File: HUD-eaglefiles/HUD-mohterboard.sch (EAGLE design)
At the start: 74 parts, among them U1 LM317, U2 ATMEGA328P_TQFP

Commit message: finalised all circuits and added comments on the motherboard circuit
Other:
- note added: "# All connectors that are going to be connected to the display board must be soldered"
- note added: "# Excese analog and digital pins each has two connectors, one is only holes for final"
- note added: "# Parts that have the value "holes" in the BOM file should only be holes."
- note added: "This is the motherboard circuit that contains the controlling circuits and connections."
- note added: "connection, the other is female header for debugging. These are soldered close to"
- note added: "eatch other."
- note added: "next to each others"

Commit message: modified the shift registers packaging
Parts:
- SR_D0, SR_D1, SR_D2: value 74595 -> 74LS595N; device SparkFun-DigitalIC:74595 -> SparkFun-DigitalIC:74LS595N
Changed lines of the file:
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@@
 <part name="DOUT" library="SparkFun-Connectors" deviceset="M05" device="PTH" value="female_header"/>
 <part name="AOUT_H" library="SparkFun-Connectors" deviceset="M06" device="SILK_FEMALE_PTH" value="holes"/>
-<part name="SR_D0" library="SparkFun-DigitalIC" deviceset="74*595" device=""/>
+<part name="SR_D0" library="SparkFun-DigitalIC" deviceset="74*595" device="N" technology="LS" value="74LS595N"/>
 <part name="GND10" library="SparkFun-Aesthetics" deviceset="GND" device=""/>
 <part name="COM_SERIAL" library="SparkFun-Connectors" deviceset="M02" device="PTH" value="male_header"/>
-<part name="SR_D1" library="SparkFun-DigitalIC" deviceset="74*595" device=""/>
+<part name="SR_D1" library="SparkFun-DigitalIC" deviceset="74*595" device="N" technology="LS" value="74LS595N"/>
 <part name="GND11" library="SparkFun-Aesthetics" deviceset="GND" device=""/>
-<part name="SR_D2" library="SparkFun-DigitalIC" deviceset="74*595" device=""/>
+<part name="SR_D2" library="SparkFun-DigitalIC" deviceset="74*595" device="N" technology="LS" value="74LS595N"/>
 <part name="GND12" library="SparkFun-Aesthetics" deviceset="GND" device=""/>
 <part name="QA0" library="SparkFun-DiscreteSemi" deviceset="TRANSISTOR_NPN" device="P2N2222A"/>

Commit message: modified the reset button into through hole packaging
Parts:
- RESET: device SmartPrj:TS42 -> SparkFun-Retired:TAC_SWITCHPTH
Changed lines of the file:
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@@
 <part name="JP1" library="SparkFun-Connectors" deviceset="M02" device="PTH" value="Pwr_in"/>
 <part name="U2" library="SparkFun-DigitalIC" deviceset="ATMEGA328P_TQFP" device="" value="ATMEGA328P_TQFP"/>
-<part name="RESET" library="SmartPrj" deviceset="TS42" device="" value="TS42031-160R-TR-7260"/>
+<part name="RESET" library="SparkFun-Retired" deviceset="TAC_SWITCH" device="PTH" value="TS42031-160R-TR-7260"/>
 <part name="GND9" library="SparkFun-Aesthetics" deviceset="GND" device=""/>
 <part name="R5" library="SparkFun-Resistors" deviceset="RESISTOR" device="PTH-1/4W" value="10K"/>
@@
 <attribute name="VALUE" x="193.04" y="187.96" size="1.778" layer="96" font="vector"/>
 </instance>
-<instance part="RESET" gate="G$1" x="167.64" y="223.52" smashed="yes">
+<instance part="RESET" gate="S" x="167.64" y="223.52" smashed="yes" rot="R90">
 <attribute name="NAME" x="161.29" y="220.98" size="1.778" layer="95" font="vector" rot="R90"/>
-<attribute name="VALUE" x="173.99" y="226.695" size="1.778" layer="96" font="vector" rot="R270"/>
+<attribute name="VALUE" x="173.99" y="212.725" size="1.778" layer="96" font="vector" rot="R90"/>
 </instance>
 <instance part="GND9" gate="1" x="170.18" y="210.82" smashed="yes">
@@
 <pinref part="GND9" gate="1" pin="GND"/>
 <wire x1="170.18" y1="213.36" x2="170.18" y2="215.9" width="0.1524" layer="91"/>
-<pinref part="RESET" gate="G$1" pin="2"/>
+<pinref part="RESET" gate="S" pin="2"/>
 <wire x1="170.18" y1="215.9" x2="170.18" y2="218.44" width="0.1524" layer="91"/>
-<pinref part="RESET" gate="G$1" pin="1"/>
+<pinref part="RESET" gate="S" pin="1"/>
 <wire x1="167.64" y1="218.44" x2="167.64" y2="215.9" width="0.1524" layer="91"/>
 <wire x1="167.64" y1="215.9" x2="170.18" y2="215.9" width="0.1524" layer="91"/>
@@
 <net name="RESET_WIRE" class="0">
 <segment>
-<pinref part="RESET" gate="G$1" pin="3"/>
+<pinref part="RESET" gate="S" pin="3"/>
 <wire x1="167.64" y1="228.6" x2="167.64" y2="231.14" width="0.1524" layer="91"/>
 <wire x1="167.64" y1="231.14" x2="170.18" y2="231.14" width="0.1524" layer="91"/>
-<pinref part="RESET" gate="G$1" pin="4"/>
+<pinref part="RESET" gate="S" pin="4"/>
 <wire x1="170.18" y1="228.6" x2="170.18" y2="231.14" width="0.1524" layer="91"/>
 <pinref part="U2" gate="U$1" pin="PC6(/RESET)"/>

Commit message: changed the transistors to uln2003 (a transistor array) and rewired the schematic
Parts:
- removed C1: 100uF, SparkFun:CAP_POLPTH1
- removed D1: 1N4001, SparkFun:DIODEPTH
- removed DIS_PWR_SELECT: JUMPER-3PTH, SparkFun-Retired:JUMPER-3PTH
- removed F1: 500mA, SparkFun:PTCPTH
- removed LED2: Power, SparkFun-Nate:LED5MM
- removed QA0, QA1, QA2, QB0, QB1, QB2, QC0, QC1, QC2, QD0, QD1, QD2, QE0, QE1, QE2, QF0, QF1, QF2, QG0, QG1, QG2: (no value), SparkFun-DiscreteSemi:TRANSISTOR_NPNP2N2222A
- removed R1: 240, SparkFun:RESISTORPTH1
- removed R10, R11, R12, R13, R14, R15, R16, R17, R18, R19, R20, R21, R22, R23, R24, R25, R26, R27, R6, R7, R8, R9: 1K, SparkFun-Resistors:RESISTORPTH-1/4W
- removed R2: 390, SparkFun:RESISTORPTH1
- removed R3, R4: 330, SparkFun:RESISTORPTH1
- removed S1: On/Off, SparkFun:SWITCH-SPSTPTH
- removed S2: Voltage, SparkFun:SWITCH-SPSTPTH
- removed U1: LM317, SparkFun:V_REG_317SINK
- added IC1: 7805TV, linear:7805TV
- added TA_D0, TA_D1, TA_D2: ULN2003AN, uln-udn:ULN2003AN
- added Y1: 4MHz, SparkFun-FreqCtrl:RESONATOR4MHZ
- C2: value 10uF -> 0.47u; device SparkFun:CAP_POLPTH2 -> SparkFun-Passives:CAP0805
- C3: value 0.1uF -> 33u; device SparkFun:CAPPTH2 -> SparkFun-Passives:CAP0805
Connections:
- removed net 12VOUT: DIS_PWR_SELECT.3, R27.2
- removed net DISPLAY_PWR-OUT: DIS_PWR_SELECT.2, PWR_PINS_OUT.1
- removed net N$20: QA1.B, R13.2
- removed net N$21: QC1.B, R15.2
- removed net N$22: QD1.B, R16.2
- removed net N$23: QE1.B, R17.2
- removed net N$24: QF1.B, R18.2
- removed net N$25: QB1.B, R14.2
- removed net N$26: QG1.B, R19.2
- removed net N$27: D1_IN.4, QD1.C
- removed net N$28: D1_IN.3, QC1.C
- removed net N$31: D1_IN.5, QE1.C
- removed net N$34: QC0.B, R8.2
- removed net N$35: QD0.B, R9.2
- removed net N$36: QE0.B, R10.2
- removed net N$37: QF0.B, R11.2
- removed net N$38: QB0.B, R7.2
- removed net N$39: QG0.B, R12.2
- removed net N$40: D0_IN.4, QD0.C
- removed net N$41: D0_IN.3, QC0.C
- removed net N$42: D0_IN.2, QB0.C
- removed net N$44: D0_IN.5, QE0.C
- removed net N$45: D0_IN.6, QF0.C
- removed net N$47: QA2.B, R20.2
- removed net N$48: QC2.B, R22.2
- removed net N$49: QD2.B, R23.2
- removed net N$50: QE2.B, R24.2
- removed net N$51: QF2.B, R25.2
- removed net N$52: QB2.B, R21.2
- removed net N$53: QG2.B, R26.2
- removed net N$54: D2_IN.4, QD2.C
- removed net PWRIN: JP1.2, S1.P
- removed net RAW: C1.+, F1.2, R27.1, U1.IN
- new net N$10: D1_IN.5, TA_D1.O5
- new net N$11: D2_IN.4, TA_D2.O4
- new net N$3: D0_IN.2, TA_D0.O2
- new net N$7: D0_IN.6, TA_D0.O6
- new net N$9: D1_IN.4, TA_D1.O4
- new net VS: C2.1, IC1.VI, JP1.2, PWR_PINS_OUT.1
- net A0: now also TA_D0.I1; no longer R6.1
- net A1: now also TA_D1.I1; no longer R13.1
- net A2: now also TA_D2.I1; no longer R20.1
- net B0: now also TA_D0.I2; no longer R7.1
- net B1: now also TA_D1.I2; no longer R14.1
- net B2: now also TA_D2.I2; no longer R21.1
- net C0: now also TA_D0.I3; no longer R8.1
- net C1: now also TA_D1.I3; no longer R15.1
- net C2: now also TA_D2.I3; no longer R22.1
- net D0: now also TA_D0.I4; no longer R9.1
- net D1: now also TA_D1.I4; no longer R16.1
- net D2: now also TA_D2.I4; no longer R23.1
- net E0: now also TA_D0.I5; no longer R10.1
- net E1: now also TA_D1.I5; no longer R17.1
- net E2: now also TA_D2.I5; no longer R24.1
- net F0: now also TA_D0.I6; no longer R11.1
- net F1: now also TA_D1.I6; no longer R18.1
- net F2: now also TA_D2.I6; no longer R25.1
- net G0: now also TA_D0.I7; no longer R12.1
- net G1: now also TA_D1.I7; no longer R19.1
- net G2: now also TA_D2.I7; no longer R26.1
- net GND: now also C2.2, IC1.GND, TA_D0.GND, TA_D1.GND, TA_D2.GND, Y1.2; no longer C1.-, C2.-, LED2.C, QA0.E, QA1.E, QA2.E, QB0.E, QB1.E, QB2.E, QC0.E, QC1.E, QC2.E, QD0.E, QD1.E, QD2.E, QE0.E, QE1.E, QE2.E, QF0.E, QF1.E, QF2.E, QG0.E, QG1.E, QG2.E, R3.1, S2.S
- net N$1: now also U2.PB6(XTAL1/TOSC1), Y1.1; no longer D1.C, F1.1
- net N$2: now also U2.PB7(XTAL2/TOSC2), Y1.3; no longer D1.A, S1.S
- net N$29: now also TA_D1.O2; no longer QB1.C
- net N$30: now also TA_D1.O1; no longer QA1.C
- net N$32: now also TA_D1.O6; no longer QF1.C
- net N$33: now also TA_D1.O7; no longer QG1.C
- net N$4: now also D0_IN.3, TA_D0.O3; no longer R2.1, R3.2, S2.P
- net N$43: now also TA_D0.O1; no longer QA0.C
- net N$46: now also TA_D0.O7; no longer QG0.C
- net N$5: now also D0_IN.4, TA_D0.O4; no longer R1.1, R2.2, U1.ADJ
- net N$55: now also TA_D2.O3; no longer QC2.C
- net N$56: now also TA_D2.O2; no longer QB2.C
- net N$57: now also TA_D2.O1; no longer QA2.C
- net N$58: now also TA_D2.O5; no longer QE2.C
- net N$59: now also TA_D2.O6; no longer QF2.C
- net N$6: now also D0_IN.5, TA_D0.O5; no longer QA0.B, R6.2
- net N$60: now also TA_D2.O7; no longer QG2.C
- net N$8: now also D1_IN.3, TA_D1.O3; no longer LED2.A, R4.1
- net VCC: now also IC1.VO; no longer C2.+, DIS_PWR_SELECT.1, R1.2, R4.2, U1.OUT
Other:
- note added: "3"
- note removed: "2"
- note removed: "Display Power Out"
- moved on the sheet: C3, D0_IN, D1_IN, D2_IN, JP1, PWR_PINS_OUT, RESET

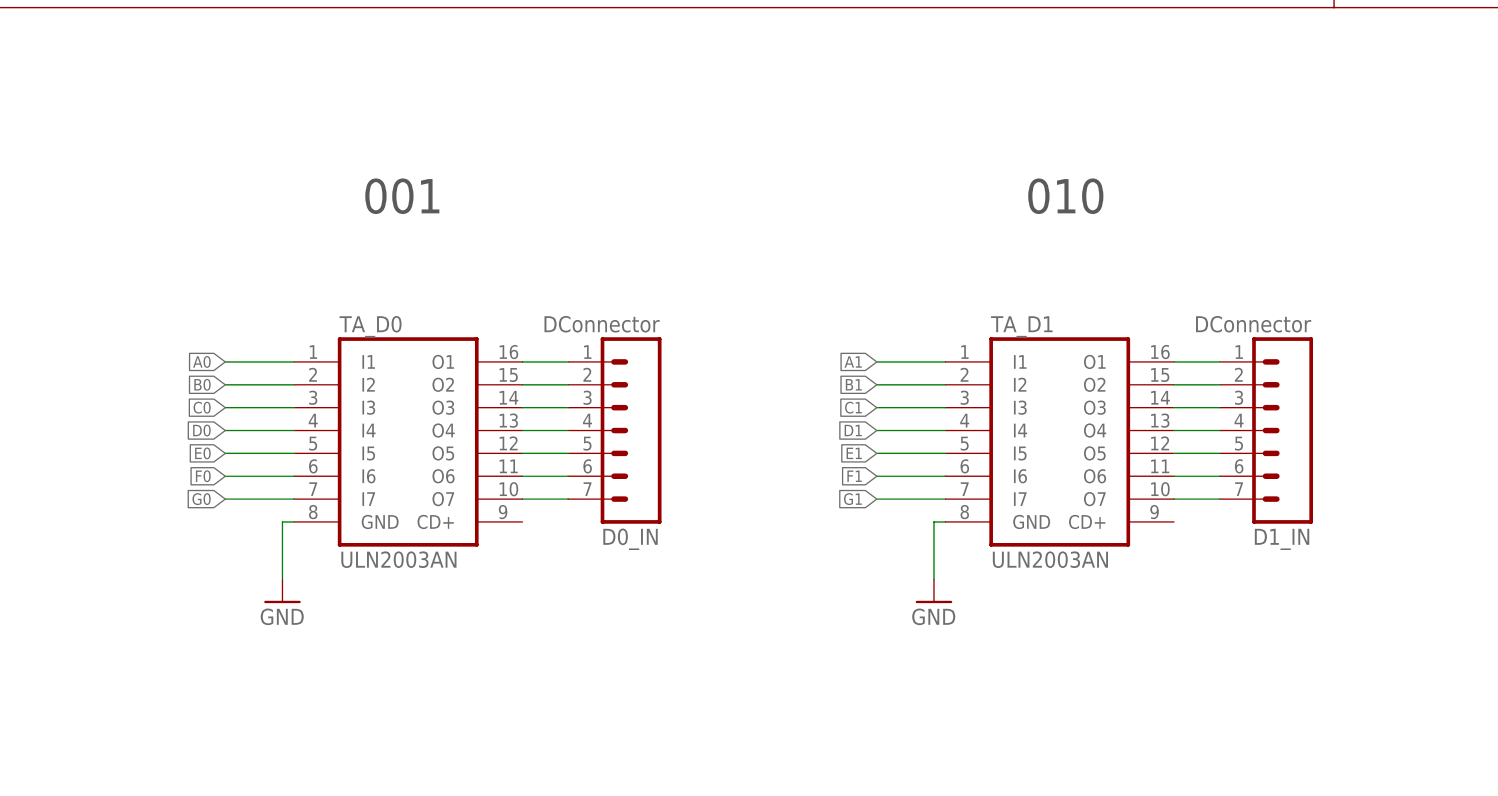
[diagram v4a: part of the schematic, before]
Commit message: added the pins mapping
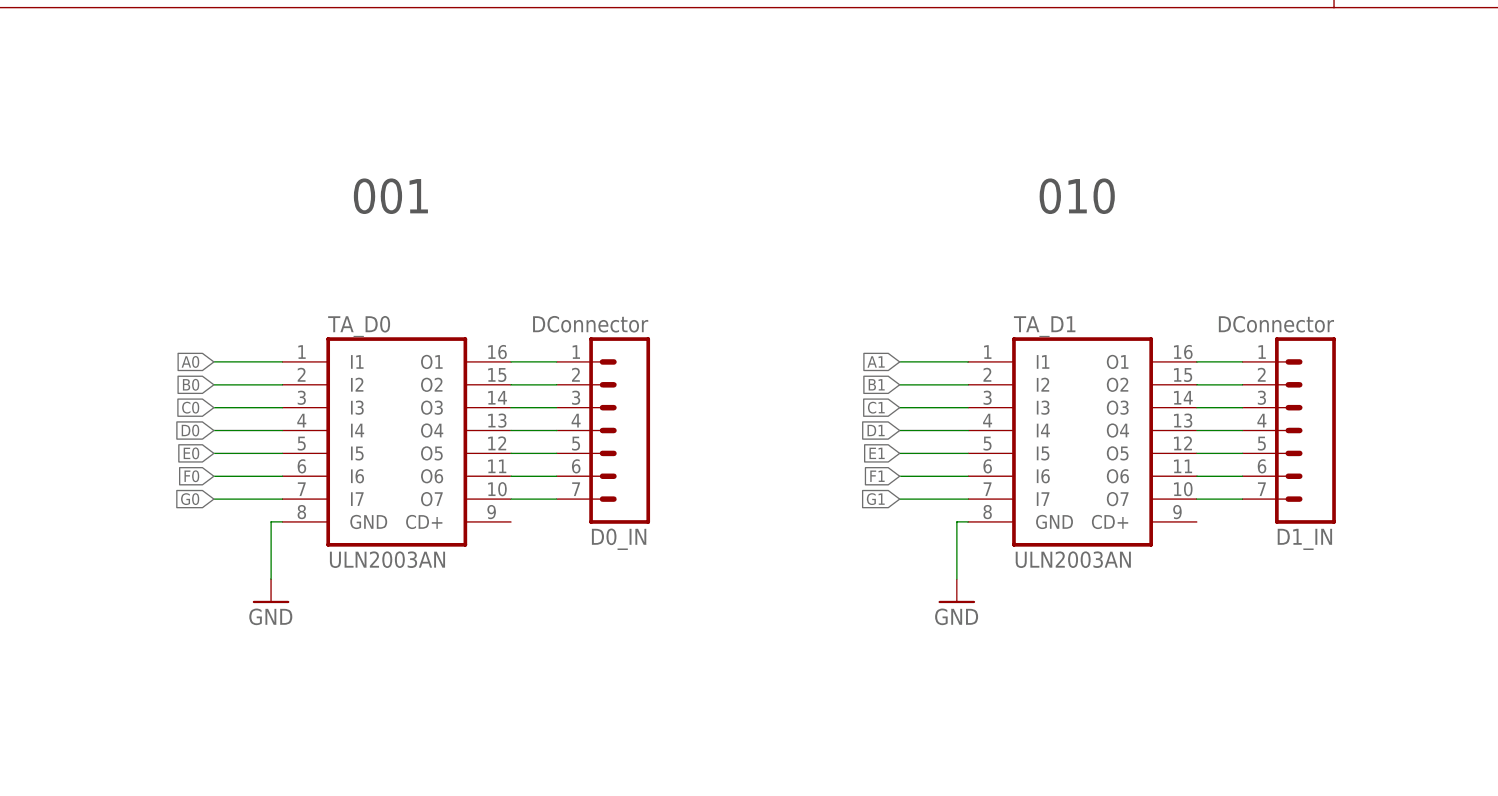
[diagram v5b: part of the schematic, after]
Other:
- note added: "OBD_RX -> D2 OBD_TX -> D3 SR_CLK -> D4 SR_SDATA -> D5 CE_D0 -> D6 CE_D1 -> D7 CE_D2 -> D8"
- moved on the sheet: D0_IN, D1_IN, TA_D0, TA_D1

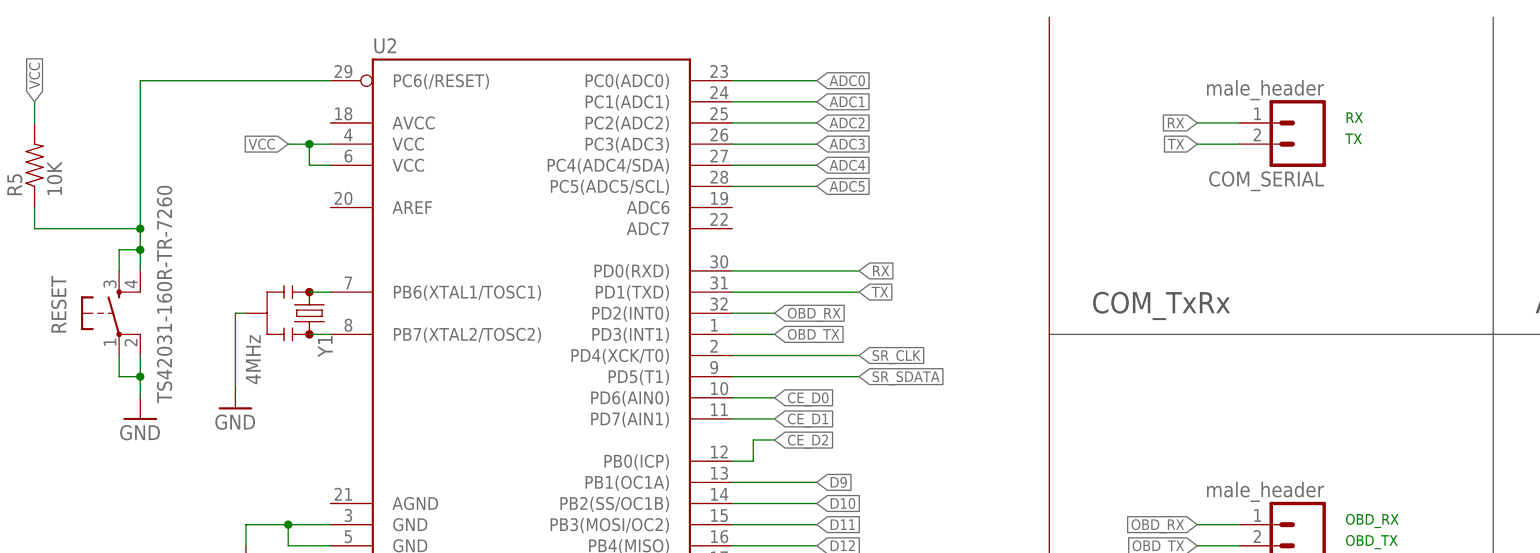
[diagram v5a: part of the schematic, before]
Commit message: fixed the serial port
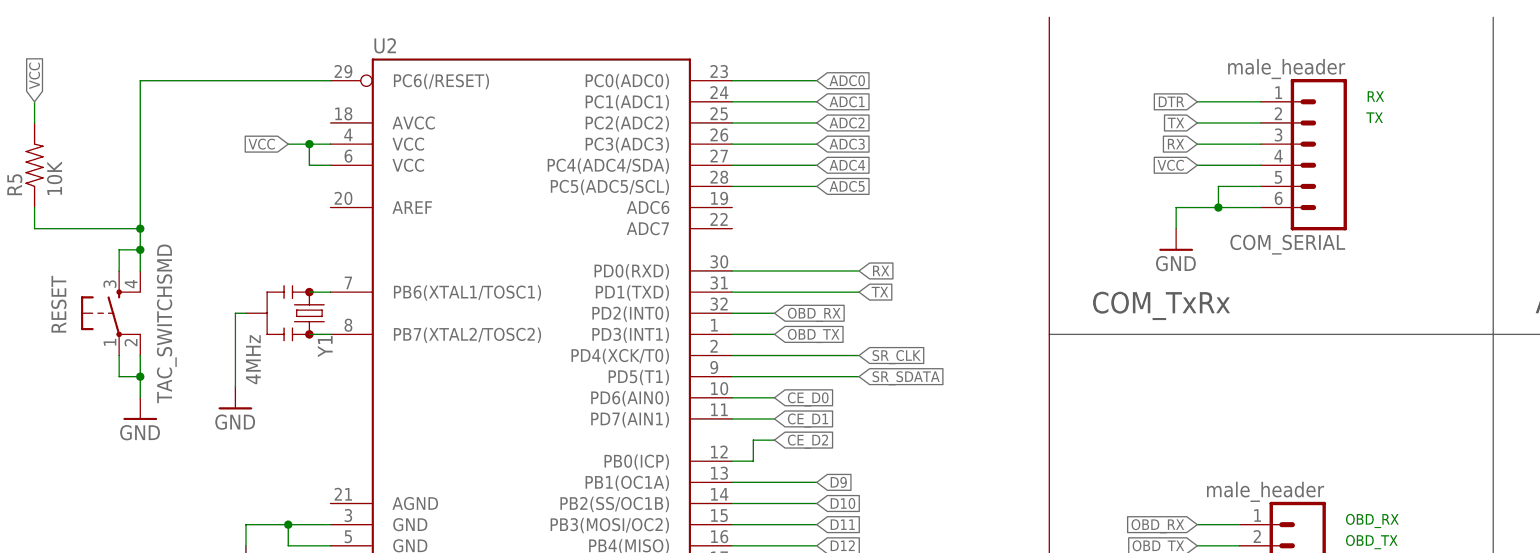
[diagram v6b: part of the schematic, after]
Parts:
- COM_SERIAL: device SparkFun-Connectors:M02PTH -> SparkFun-Connectors:M06SILK_FEMALE_PTH
- R5: device SparkFun-Resistors:RESISTORPTH-1/4W -> SparkFun-Resistors:RESISTOR0805-RES
- RESET: value TS42031-160R-TR-7260 -> TAC_SWITCHSMD; device SparkFun-Retired:TAC_SWITCHPTH -> SparkFun-Retired:TAC_SWITCHSMD
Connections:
- new net DTR: COM_SERIAL.1
- net GND: now also COM_SERIAL.5, COM_SERIAL.6
- net RX: now also COM_SERIAL.3; no longer COM_SERIAL.1
- net VCC: now also COM_SERIAL.4
